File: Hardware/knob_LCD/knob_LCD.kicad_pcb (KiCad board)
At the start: 2 copper layers, 50 x 49.3 mm, 14 parts, among them J1 ST77903, J3 Conn_01x14_Socket, Q1 AO3400A

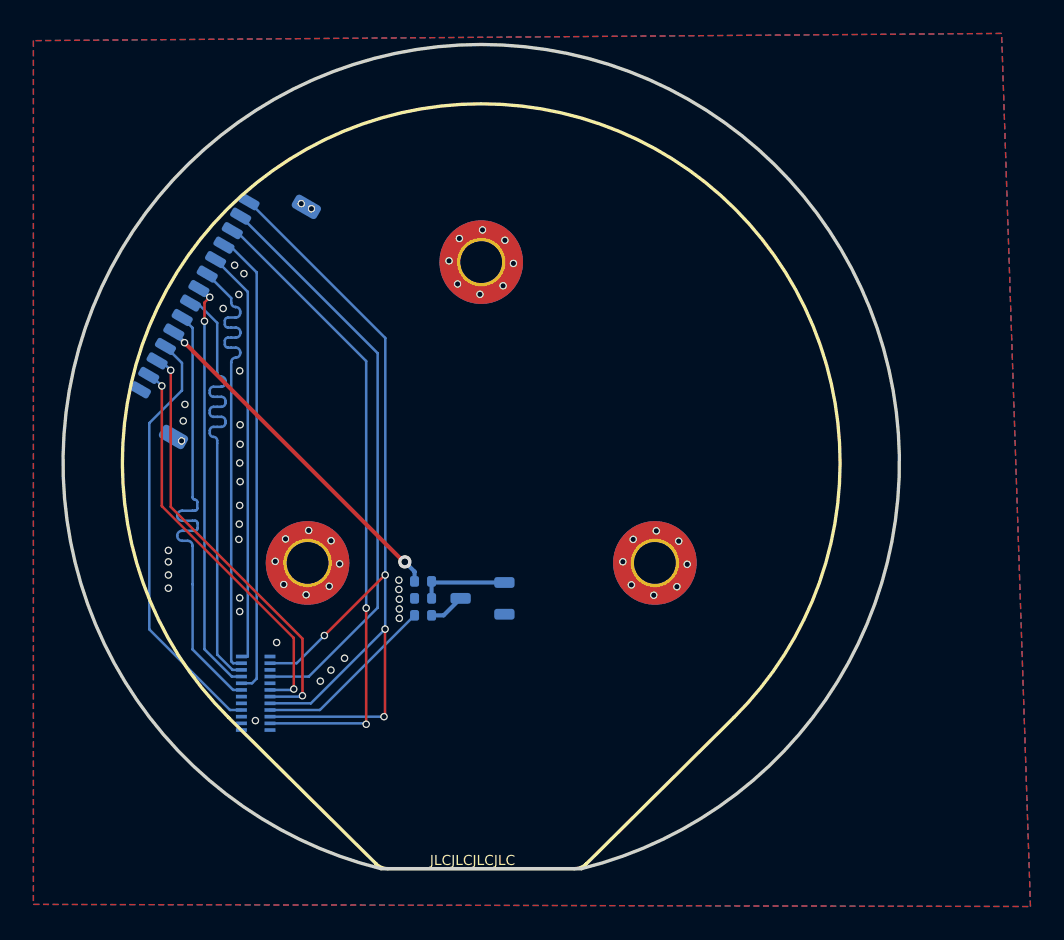
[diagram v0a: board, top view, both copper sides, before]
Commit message: fix socket pinout
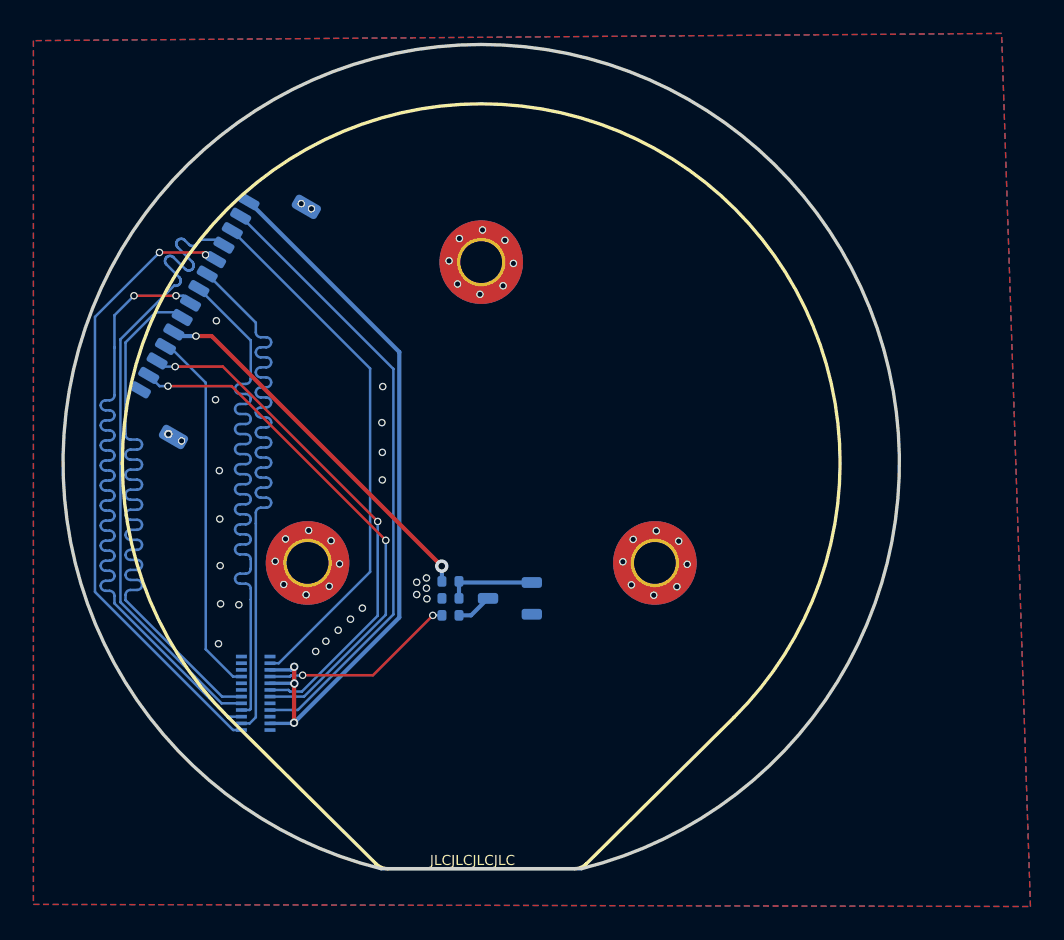
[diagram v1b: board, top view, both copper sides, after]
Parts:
- moved Q1 1.64 mm to (146.8, 106.0)
- moved R1 1.64 mm to (143.2, 105.0)
- moved R2 1.64 mm to (143.2, 106.0)
- moved R3 1.64 mm to (143.2, 107.0)
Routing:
- net /LCD_D1: track 27.9 -> 43.7 mm, vias 0 -> 2
- net /LCD_CLK: track 25.0 -> 40.2 mm, vias 2 -> 0
- net +3V3: track 58.9 -> 45.3 mm, vias 4 -> 3
- net /LCD_CS: track 24.9 -> 37.6 mm, vias 0 -> 2
- net /LCD_D2: track 27.9 -> 40.3 mm
- net /LCD_D0: track 27.8 -> 40.2 mm
- net /LCD_D3: track 28.0 -> 39.7 mm
- net /TP_SDA: track 23.9 -> 31.7 mm
- net /LCD_TE: track 38.8 -> 32.1 mm, vias 2 -> 0
- net /TP_SCL: track 25.8 -> 31.2 mm
- net /LCD_RST: track 25.7 -> 22.1 mm
- net /TP_RST: track 35.0 -> 37.4 mm
- net /LCD_BLK: track 20.9 -> 22.8 mm
- net /LEDK: track 11.2 -> 11.8 mm, vias 0 -> 2
- net GND: vias 57 -> 50

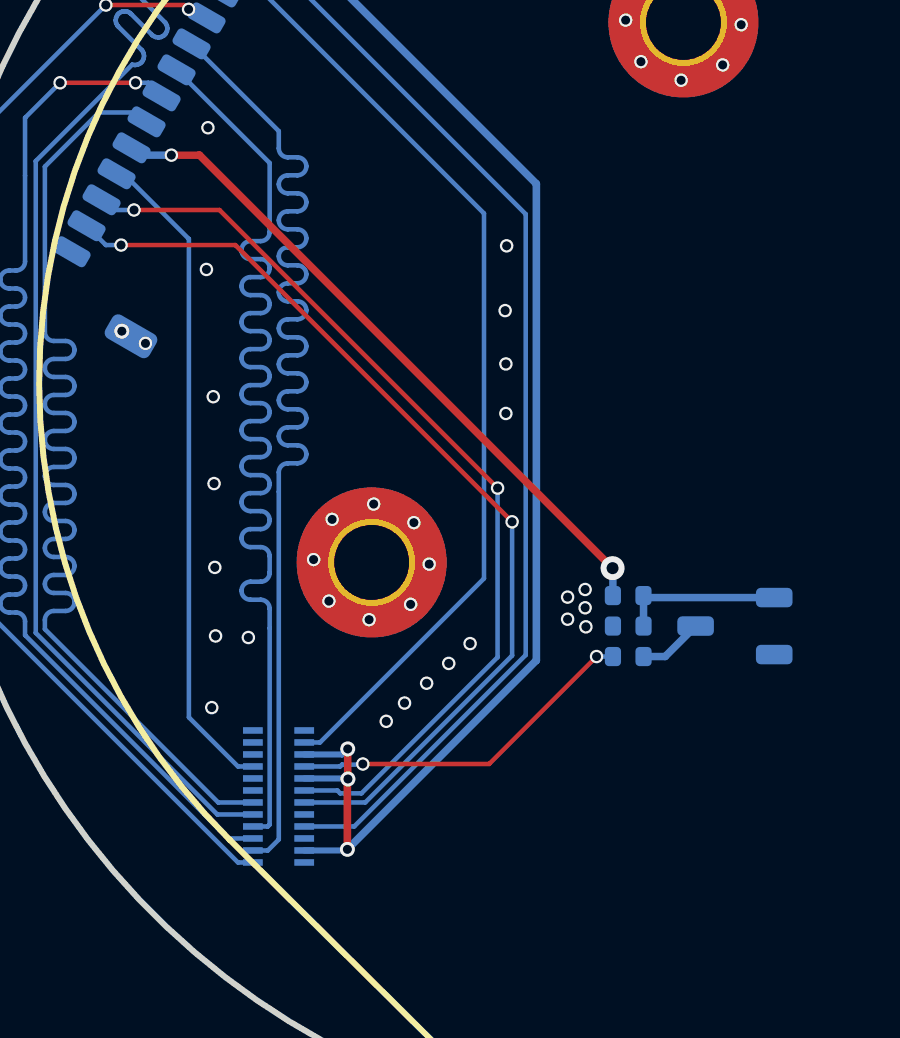
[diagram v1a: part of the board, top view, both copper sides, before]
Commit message: CH224K & ST77903 symbol fix
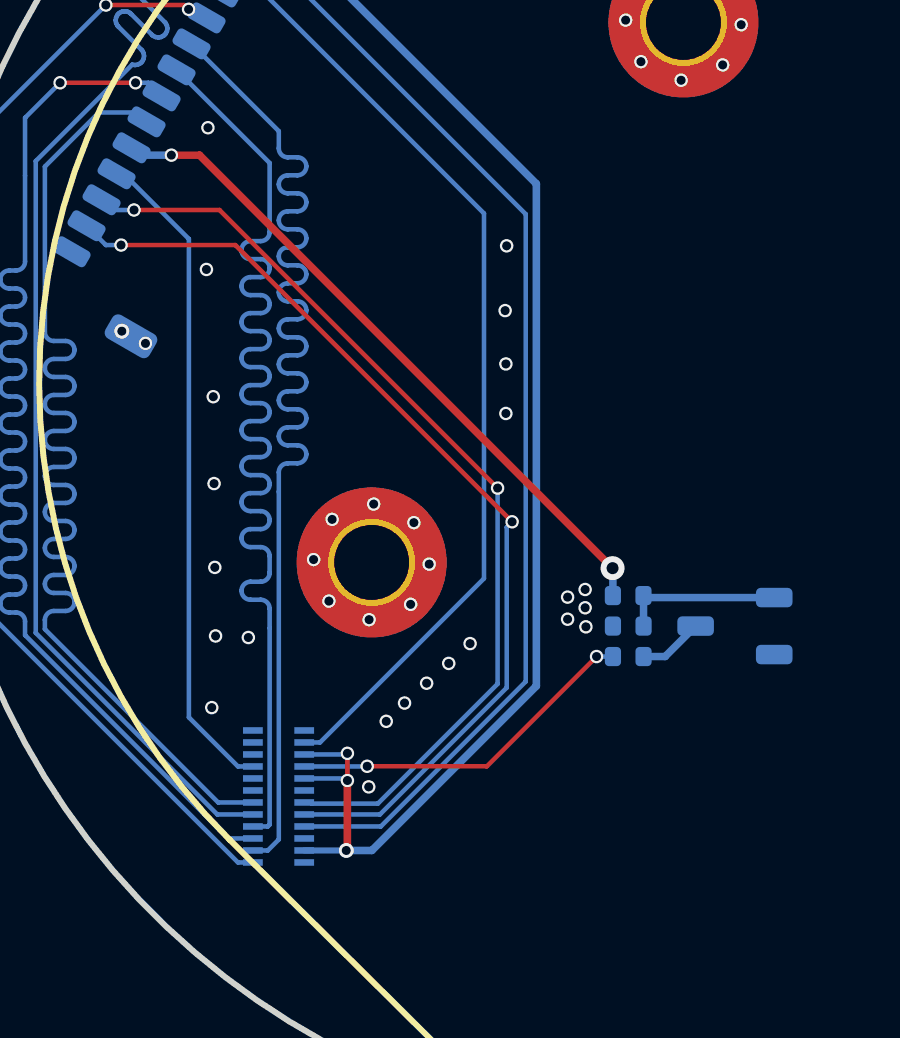
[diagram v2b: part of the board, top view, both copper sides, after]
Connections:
- J1 pad 18: /TP_SCL -> GND
- J1 pad 19: /TP_SDA -> /TP_SCL
- J1 pad 20: (no net) -> /TP_SDA
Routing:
- net /TP_SDA: track 31.7 -> 32.4 mm
- net /TP_SCL: track 31.2 -> 31.8 mm
- net /TP_RST: track 37.4 -> 37.9 mm
- net GND: vias 50 -> 51
